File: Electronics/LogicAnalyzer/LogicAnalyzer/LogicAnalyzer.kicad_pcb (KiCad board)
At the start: 2 copper layers, 57 x 55.2 mm, 10 parts, among them J1 Conn_02x15_Odd_Even, J2 Conn_01x03, J3 Conn_01x03, U1 Pico

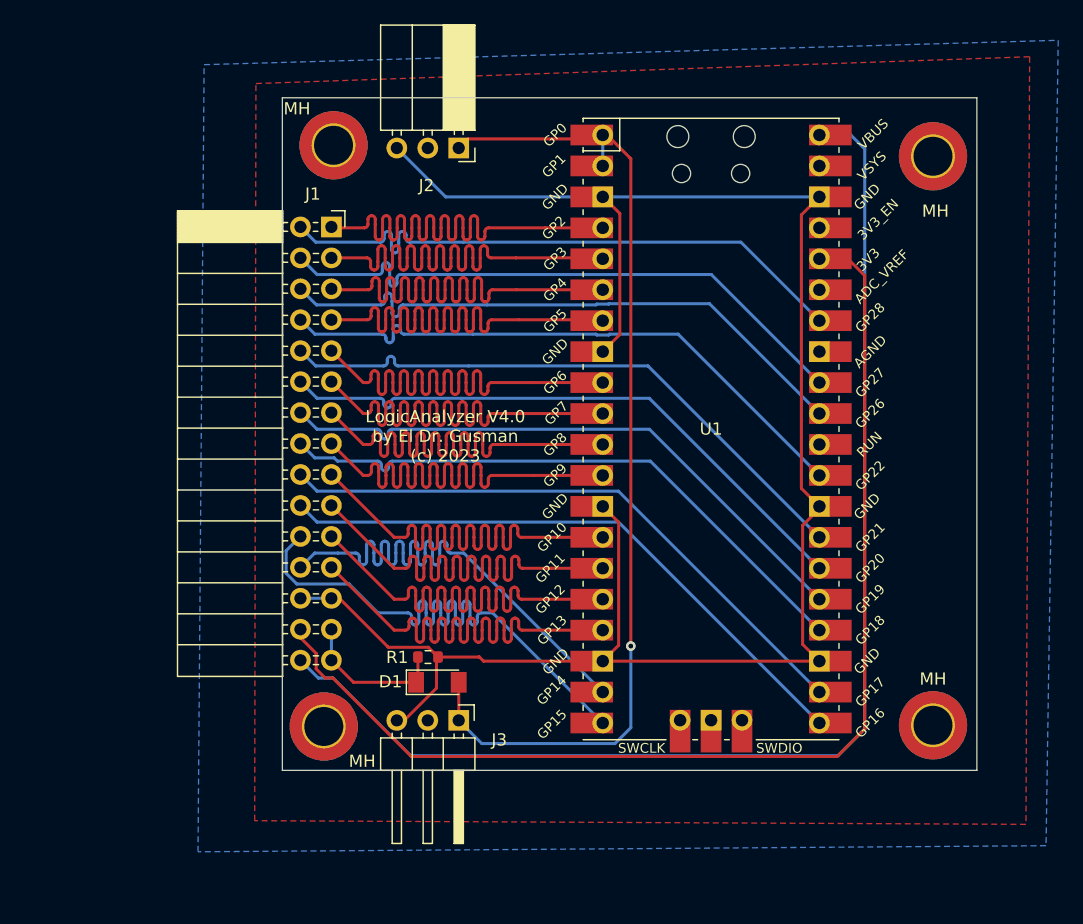
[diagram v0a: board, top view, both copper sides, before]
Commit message: Version 5.0 of PCB
- Integrated bidirectional voltage translators
- Added Power LED
- Switchable internal or external reference voltage
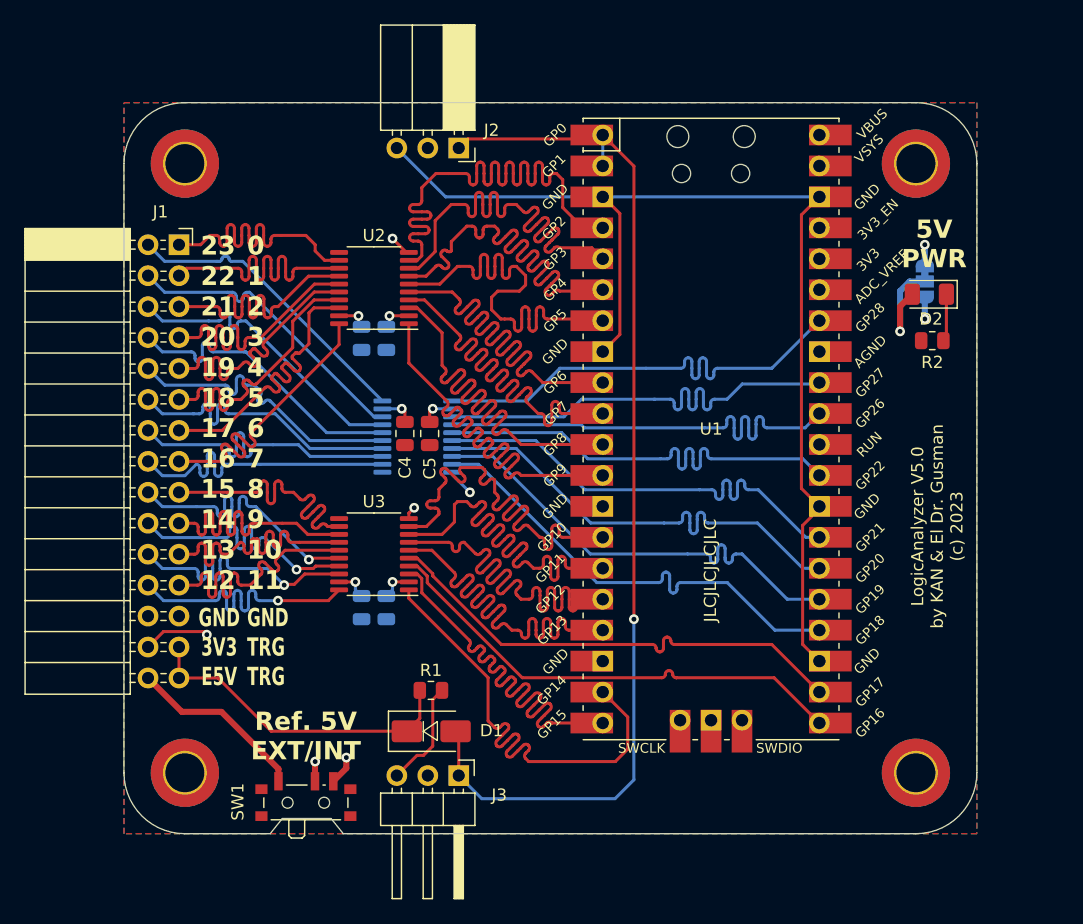
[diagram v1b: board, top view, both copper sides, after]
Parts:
- removed MH (x4): MountingHole_3.2mm_M3_DIN965_Pad_TopBottom, MountingHole:MountingHole_3.2mm_M3_DIN965_Pad_TopBottom
- added C1: C, Capacitor_SMD:C_0805_2012Metric, B.Cu at (81.5, 103.4)
- added C2: C, Capacitor_SMD:C_0805_2012Metric, B.Cu at (79.5, 81.3)
- added C3: C, Capacitor_SMD:C_0805_2012Metric, B.Cu at (81.5, 81.3)
- added C4: C, Capacitor_SMD:C_0805_2012Metric, F.Cu at (83.1, 89.2)
- added C5: C, Capacitor_SMD:C_0805_2012Metric, F.Cu at (85.1, 89.2)
- added C6: C, Capacitor_SMD:C_0805_2012Metric, B.Cu at (79.5, 103.4)
- added D2: LED, LED_SMD:LED_1206_3216Metric, F.Cu at (126.1, 77.7)
- added H1: MountingHole, MountingHole:MountingHole_3.2mm_M3_DIN965_Pad_TopBottom, F.Cu at (65.0, 67.0)
- added H2: MountingHole, MountingHole:MountingHole_3.2mm_M3_DIN965_Pad_TopBottom, F.Cu at (125.0, 67.0)
- added H3: MountingHole, MountingHole:MountingHole_3.2mm_M3_DIN965_Pad_TopBottom, F.Cu at (125.0, 117.0)
- added H4: MountingHole, MountingHole:MountingHole_3.2mm_M3_DIN965_Pad_TopBottom, F.Cu at (65.0, 117.0)
- added JP1: VBus/VSys, Jumper:SolderJumper-3_P1.3mm_Bridged12_RoundedPad1.0x1.5mm, B.Cu at (125.7, 76.7)
- added R2: 330, Resistor_SMD:R_0805_2012Metric, F.Cu at (126.3, 81.5)
- added SW1: SW_SPDT, Button_Switch_SMD:SW_SPDT_PCM12, F.Cu at (74.9, 119.1)
- added U2: TXB0108PWR, Package_SO:TSSOP-20_4.4x6.5mm_P0.65mm, F.Cu at (80.5, 77.2)
- added U3: TXB0108PWR, Package_SO:TSSOP-20_4.4x6.5mm_P0.65mm, F.Cu at (80.5, 99.1)
- added U4: TXB0108PWR, Package_SO:TSSOP-20_4.4x6.5mm_P0.65mm, B.Cu at (84.1, 89.4)
- D1: footprint Diode_SMD:D_MiniMELF -> Diode_SMD:D_SMA
- R1: footprint Resistor_SMD:R_0603_1608Metric -> Resistor_SMD:R_0805_2012Metric
- moved J1 12.6 mm to (64.5, 73.7)
- moved J3 4.53 mm to (87.5, 117.2)
- moved D1 4.05 mm to (85.2, 113.6)
- moved R1 2.75 mm to (85.2, 110.2)
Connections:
- net /3V3 renamed +3.3V
- net /GND renamed GND
- J1 pad 1: /CHAN_0 -> /CHAN_0_OUT
- J1 pad 10: /CHAN_19 -> /CHAN_19_OUT
- J1 pad 11: /CHAN_5 -> /CHAN_5_OUT
- J1 pad 12: /CHAN_18 -> /CHAN_18_OUT
- J1 pad 13: /CHAN_6 -> /CHAN_6_OUT
- J1 pad 14: /CHAN_17 -> /CHAN_17_OUT
- J1 pad 15: /CHAN_7 -> /CHAN_7_OUT
- J1 pad 16: /CHAN_16 -> /CHAN_16_OUT
- J1 pad 17: /CHAN_8 -> /CHAN_8_OUT
- J1 pad 18: /CHAN_15 -> /CHAN_15_OUT
- J1 pad 19: /CHAN_9 -> /CHAN_9_OUT
- J1 pad 2: /CHAN_23 -> /CHAN_23_OUT
- J1 pad 20: /CHAN_14 -> /CHAN_14_OUT
- J1 pad 21: /CHAN_10 -> /CHAN_10_OUT
- J1 pad 22: /CHAN_13 -> /CHAN_13_OUT
- J1 pad 23: /CHAN_11 -> /CHAN_11_OUT
- J1 pad 24: /CHAN_12 -> /CHAN_12_OUT
- J1 pad 3: /CHAN_1 -> /CHAN_1_OUT
- J1 pad 30: /5V -> +5V
- J1 pad 4: /CHAN_22 -> /CHAN_22_OUT
- J1 pad 5: /CHAN_2 -> /CHAN_2_OUT
- J1 pad 6: /CHAN_21 -> /CHAN_21_OUT
- J1 pad 7: /CHAN_3 -> /CHAN_3_OUT
- J1 pad 8: /CHAN_20 -> /CHAN_20_OUT
- J1 pad 9: /CHAN_4 -> /CHAN_4_OUT
- U1 pad 39: unconnected-(U1-Pad39) -> Net-(JP1-B)
- U1 pad 40: /5V -> Net-(JP1-A)
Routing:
- net /5V: track 102.3 -> 0.00 mm
- net VBUS: track 0.00 -> 94.2 mm, vias 0 -> 2
- net +3.3V: track 94.2 -> 18.7 mm, vias 0 -> 7
- net GND: track 156.7 -> 100.3 mm
- net VCCQ: track 0.00 -> 50.7 mm, vias 0 -> 4
- net /CHAN_22_OUT: track 0.00 -> 25.0 mm
- net /CHAN_23_OUT: track 0.00 -> 25.0 mm
- net /CHAN_21_OUT: track 0.00 -> 24.9 mm
- net /CHAN_20_OUT: track 0.00 -> 24.9 mm
- net /CHAN_18_OUT: track 0.00 -> 24.9 mm
- net /CHAN_17_OUT: track 0.00 -> 24.9 mm
- net /CHAN_16_OUT: track 0.00 -> 24.9 mm
- net /CHAN_6_OUT: track 0.00 -> 24.9 mm
- net /CHAN_7_OUT: track 0.00 -> 24.9 mm
- net /CHAN_19_OUT: track 0.00 -> 24.9 mm
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- added copper zone on In2.Cu, net +3.3V
- added copper zone on In1.Cu, net GND
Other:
- board size 57 x 55.2 mm -> 70 x 60 mm
- copper layers 2 -> 4
- board text added: "(Backfeed Protected)"
- board text added: "0 1 2 3 4 5 6 7 8 9 10 11"
- board text added: "23 22 21 20 19 18 17 16 15 14 13 12"
- board text added: "5V PWR"
- board text added: "GND 3V3 E5V"
- board text added: "GND TRG TRG"
- board text added: "JLCJLCJLCJLC"
- board text added: "LogicAnalyzer V5.0 by KAN & El Dr. Gusman (c) 2023"
- board text added: "Ref. 5V EXT/INT"
- board text added: "Ref. 5V INT/EXT"
- board text added: "VBUS"
- board text added: "VSYS"
- board text removed: "LogicAnalyzer V4.0 by El Dr. Gusman (c) 2023"
